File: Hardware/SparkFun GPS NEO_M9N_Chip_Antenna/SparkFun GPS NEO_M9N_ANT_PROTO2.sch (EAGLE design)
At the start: 50 parts, among them J2 Qwiic Right Angle, U1 U-BLOX_NEO-M9N, U2 3.3V, Y1 GPS_CHIP_ANTENNAW3011

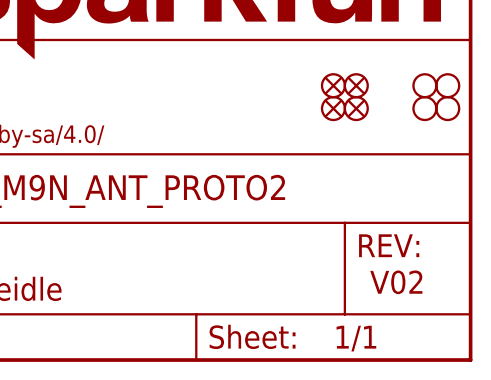
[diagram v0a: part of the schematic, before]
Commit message: Changes version on single-qwiic board to v03
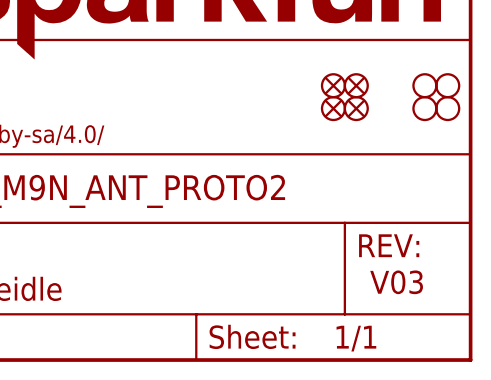
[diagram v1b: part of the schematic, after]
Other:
- note added: "V03"
- note removed: "V02"
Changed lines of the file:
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@@
 <sheet>
 <plain>
-<text x="237.744" y="7.366" size="2.54" layer="94" font="vector">V02</text>
+<text x="237.744" y="7.366" size="2.54" layer="94" font="vector">V03</text>
 <text x="55.88" y="119.38" size="1.778" layer="97" font="vector" align="center">7-bit unshifted I2C address: 0x42</text>
 <wire x1="0" y1="106.68" x2="73.66" y2="106.68" width="0.1524" layer="97" style="shortdash"/>
